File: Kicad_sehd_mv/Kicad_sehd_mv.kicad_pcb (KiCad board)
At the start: 2 copper layers, 1 part, among them J1 Conn_02x06_Top_Bottom

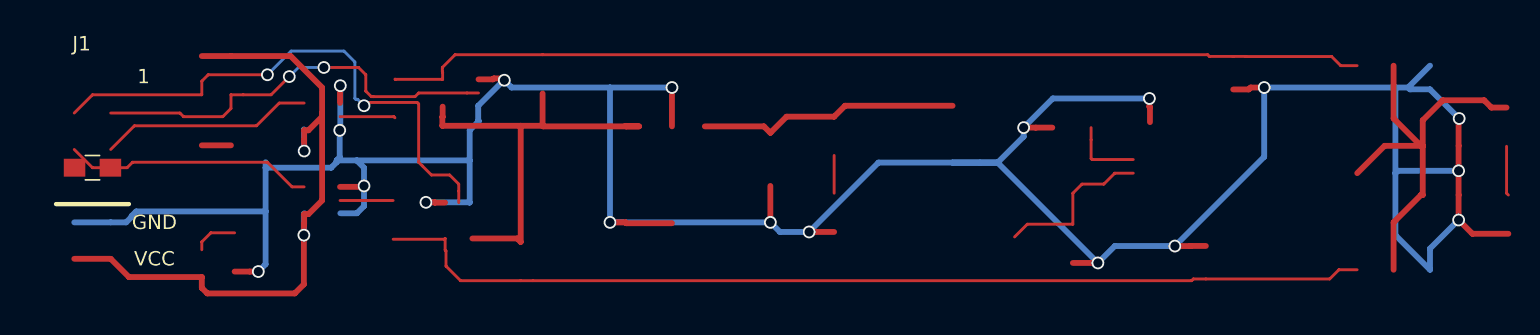
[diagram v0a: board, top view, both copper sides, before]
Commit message: Order PCB of Kicad_sehd_mv
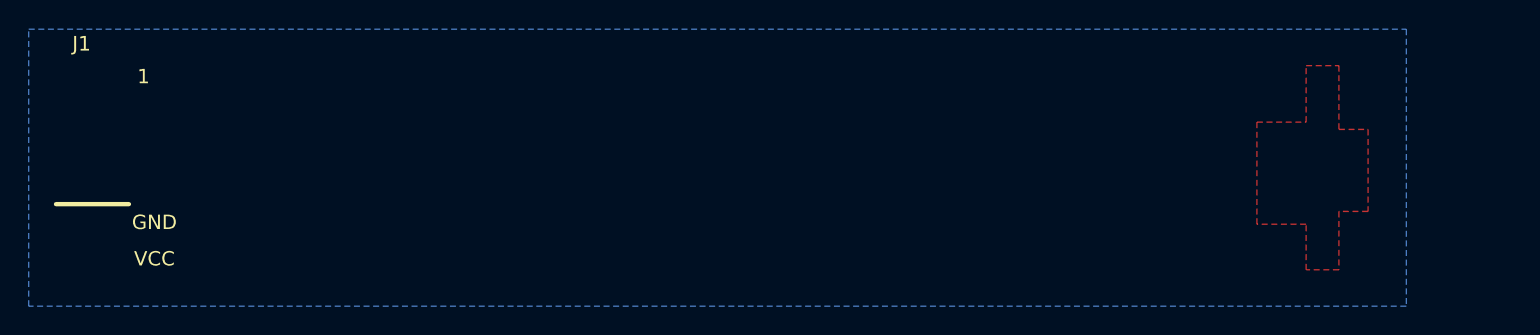
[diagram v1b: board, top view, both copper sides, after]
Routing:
- net GND: track 234.2 -> 0.00 mm, vias 18 -> 0
- net Net-(IC4-Pad4): track 69.8 -> 0.00 mm
- net Net-(IC3-Pad4): track 68.6 -> 0.00 mm
- net VCC: track 49.9 -> 0.00 mm, vias 2 -> 0
- net Net-(IC4-Pad2): track 38.3 -> 0.00 mm, vias 2 -> 0
- net +5V: track 29.9 -> 0.00 mm
- net VDD: track 29.8 -> 0.00 mm
- net Net-(IC3-Pad2): track 29.3 -> 0.00 mm, vias 2 -> 0
- net VDDA: track 18.2 -> 0.00 mm
- net Net-(IC6-Pad4): track 17.4 -> 0.00 mm
- net Net-(IC5-Pad4): track 14.8 -> 0.00 mm
- net Net-(IC1-Pad5): track 11.4 -> 0.00 mm
- net Net-(IC1-Pad4): track 5.13 -> 0.00 mm
- net Net-(IC5-Pad2): track 3.86 -> 0.00 mm
- net Net-(IC6-Pad2): track 3.70 -> 0.00 mm
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- added copper zone on B.Cu, net GND
- added copper zone on F.Cu, net VDD
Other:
- net class OutSignal added: clearance 0.2032, trace_width 0.4064, via_dia 0.889, via_drill 0.635
